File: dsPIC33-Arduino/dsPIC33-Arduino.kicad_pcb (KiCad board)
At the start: 2 copper layers, 68.6 x 53.3 mm, 8 parts, among them P1 Power, P2 Analog, P3 Digital, P4 Digital, P5 CONN_1, P6 CONN_1, P7 CONN_1, P8 CONN_1

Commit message: wip
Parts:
- added C1: 100nF, Capacitors_SMD:C_0805_HandSoldering, F.Cu at (118.7, 97.0)
- added C10: 100nF, Capacitors_ThroughHole:C_Disc_D3_P2.5, F.Cu at (138.2, 97.0)
- added C11: CP, w_capacitors:CP_4x5mm, F.Cu at (161.2, 92.4)
- added C12: 22pF, Capacitors_ThroughHole:C_Disc_D3_P2.5, F.Cu at (157.3, 114.7)
- added C13: 22pF, Capacitors_ThroughHole:C_Disc_D3_P2.5, F.Cu at (162.4, 114.4)
- added C14: 100nF, Capacitors_SMD:C_0805_HandSoldering, F.Cu at (115.3, 104.4)
- added C15: 100nF, Capacitors_SMD:C_0805_HandSoldering, F.Cu at (115.1, 109.1)
- added C2: 4,7uF, Capacitors_SMD:C_0805_HandSoldering, F.Cu at (118.7, 99.3)
- added C3: 10nF, Capacitors_SMD:C_0805_HandSoldering, F.Cu at (126.8, 84.7)
- added C4: 47pF, Capacitors_SMD:C_0805_HandSoldering, F.Cu at (124.1, 92.8)
- added C5: 47pF, Capacitors_SMD:C_0805_HandSoldering, F.Cu at (123.9, 95.0)
- added C6: 100nF, Capacitors_SMD:C_0805_HandSoldering, F.Cu at (124.9, 80.8)
- added C7: 100nF, Capacitors_SMD:C_0805_HandSoldering, F.Cu at (124.0, 97.4)
- added C8: 100nF, Capacitors_SMD:C_0805_HandSoldering, F.Cu at (127.5, 94.5)
- added C9: 100nF, Capacitors_ThroughHole:C_Disc_D3_P2.5, F.Cu at (132.8, 124.3)
- added CON1: BARREL_JACK, Connect:BARREL_JACK, F.Cu at (115.3, 118.7)
- added D1: RX LED, LEDs:LED_0805, F.Cu at (135.8, 78.7)
- added D2: TX LED, LEDs:LED_0805, F.Cu at (135.8, 80.6)
- added D3: Power LED, LEDs:LED-3MM, F.Cu at (142.1, 81.4)
- added D4: BAT43, w_pth_diodes:diode_do35, F.Cu at (141.7, 116.5)
- added D5: LED, LEDs:LED-3MM, F.Cu at (166.8, 93.0)
- added D6: D, w_pth_diodes:diode_do35, F.Cu at (141.7, 110.0)
- added F1: Ferrit, Resistors_SMD:R_0805_HandSoldering, F.Cu at (118.4, 80.5)
- added JP1: ICSP, ICSP:ICSP, F.Cu at (134.9, 116.0)
- added P10: CONN_01X03, Pin_Headers:Pin_Header_Straight_1x03, F.Cu at (175.8, 106.6)
- added P11: CONN_01X03, Pin_Headers:Pin_Header_Straight_1x03, F.Cu at (152.0, 91.1)
- added P12: CONN_01X04, Socket_Strips:Socket_Strip_Straight_1x04, F.Cu at (130.5, 112.5)
- added P13: CONN_01X02, Socket_Strips:Socket_Strip_Straight_2x01, F.Cu at (172.7, 117.0)
- added P14: Power Select, Socket_Strips:Socket_Strip_Straight_1x03, F.Cu at (140.2, 89.9)
- added P15: Grove I2C, w_conn_jst-ph:s4b-ph-kl, F.Cu at (173.2, 83.2)
- added P9: USB_B, Connect:USB_B, F.Cu at (119.4, 89.5)
- added R1: 27, Resistors_SMD:R_0805_HandSoldering, F.Cu at (123.6, 82.4)
- added R10: 0, Resistors_SMD:R_0805_HandSoldering, F.Cu at (124.0, 99.7)
- added R2: 27, Resistors_SMD:R_0805_HandSoldering, F.Cu at (132.1, 84.8)
- added R3: 270, Resistors_SMD:R_0805_HandSoldering, F.Cu at (131.4, 78.7)
- added R4: 270, Resistors_SMD:R_0805_HandSoldering, F.Cu at (131.4, 80.6)
- added R5: 1k5, w_pth_resistors:RC03, F.Cu at (141.9, 92.9)
- added R6: 470, w_pth_resistors:RC03, F.Cu at (141.7, 118.9)
- added R7: 4k7, w_pth_resistors:RC03, F.Cu at (142.0, 112.3)
- added R8: 4k7, Resistors_SMD:R_0805_HandSoldering, F.Cu at (129.5, 101.1)
- added R9: 1k5, w_pth_resistors:RC03, F.Cu at (167.9, 96.2)
- added SW1: SW_PUSH, Buttons_Switches_ThroughHole:SW_PUSH_SMALL, F.Cu at (117.1, 76.8)
- added U1: FT230XS, w_smd_dil:ssop-16, F.Cu at (125.4, 88.5)
- added U2: LM1117 3V3, TO_SOT_Packages_SMD:SOT-223, F.Cu at (122.3, 108.6)
- added U3: dsPIC33EVxxxGM102-I/SP, w_pth_circuits:dil_28-300_socket, F.Cu at (154.6, 102.9)
- added U4: 74LVC1G32, TO_SOT_Packages_SMD:SOT-353, F.Cu at (125.9, 103.0)
- added U5: LM1117 5V, TO_SOT_Packages_SMD:SOT-223, F.Cu at (128.3, 118.5)
- added Y1: Crystal, w_crystal:crystal_hc-49s, F.Cu at (159.8, 111.0)
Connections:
- net /A4(SDA) renamed /SDA
- net /A5(SCL) renamed /SCL
- P1 pad 2: /IOREF -> VDD
- P1 pad 3: /Reset -> /~RESET~
- P1 pad 8: /Vin -> +5V
- P4 pad 7: /1(Tx) -> /TX
- P4 pad 8: /0(Rx) -> /RX

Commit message: wip
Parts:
- added P16: PIN19, Pin_Headers:Pin_Header_Straight_1x03, F.Cu at (156.7, 93.3)
- added P17: UART/CAN, w_conn_jst-ph:s4b-ph-kl, F.Cu at (173.2, 82.5)
- P10: value CONN_01X03 -> PIN20
- P11: value CONN_01X03 -> PIN5
- P12: value CONN_01X04 -> PWR_IN; footprint Socket_Strips:Socket_Strip_Straight_1x04 -> Pin_Headers:Pin_Header_Straight_1x03
- P13: value CONN_01X02 -> PIN2
- P15: value Grove I2C -> I2C
- moved P13 48.7 mm to (134.1, 87.2), turned to 270 degrees
- moved JP1 40.1 mm to (173.2, 104.1)
- moved P10 28.5 mm to (152.9, 89.5), turned to 90 degrees
- moved P15 27.9 mm to (173.2, 111.1)
- moved C9 22.1 mm to (132.6, 102.2), turned to 270 degrees
- moved R9 20.2 mm to (165.0, 116.2), turned to 90 degrees
- moved P11 19.3 mm to (144.0, 108.6)
- moved D5 14.3 mm to (166.2, 107.3), turned to 270 degrees
- moved P14 12.4 mm to (132.6, 99.7), turned to 90 degrees
- moved R8 8.46 mm to (121.2, 102.2)
- moved D6 7.33 mm to (134.5, 111.1), turned to 90 degrees
- moved P12 7.28 mm to (129.5, 105.3), turned to 0 degrees
- moved D4 7.11 mm to (137.0, 111.1), turned to 90 degrees
- moved Y1 3.05 mm to (158.0, 108.6)
- moved C10 3.00 mm to (136.4, 94.6)
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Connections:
- P15 pad 1: /SCL -> GND
- P15 pad 2: /SDA -> VDD
- P15 pad 3: VDD -> /SDA
- P15 pad 4: GND -> /SCL
- U3 pad 19: GND -> Net-(P16-Pad2)
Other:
- board text added: "GND"
- board text added: "RX"
- board text added: "SCL"
- board text added: "SDA"
- board text added: "TX"
- board text added: "VDD"

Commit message: wip
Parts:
- D6: value D -> BAT43
- P13: footprint Socket_Strips:Socket_Strip_Straight_2x01 -> Pin_Headers:Pin_Header_Straight_1x02
- P14: footprint Socket_Strips:Socket_Strip_Straight_1x03 -> Pin_Headers:Pin_Header_Straight_1x03
- moved C9 31.0 mm to (163.1, 108.1), turned to 0 degrees
- moved R8 22.5 mm to (134.7, 84.3)
- moved C8 22.1 mm to (133.9, 115.7), turned to 270 degrees
- moved C2 20.9 mm to (124.3, 79.2)
- moved D6 20.6 mm to (137.7, 90.8)
- moved U5 17.8 mm to (115.6, 105.5), turned to 90 degrees
- moved U4 17.6 mm to (134.5, 87.6)
- moved C1 16.4 mm to (124.3, 81.5)
- moved C7 16.4 mm to (133.9, 110.5), turned to 90 degrees
- moved F1 15.4 mm to (124.2, 94.7), turned to 180 degrees
- moved C10 15.2 mm to (151.5, 93.5)
- moved P11 15.1 mm to (143.4, 93.5)
- moved C6 12.7 mm to (127.8, 93.2), turned to 270 degrees
- moved P12 11.7 mm to (120.5, 97.8), turned to 90 degrees
- moved R10 10.5 mm to (113.8, 97.3)
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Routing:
- net Net-(P9-Pad5): track 0.00 -> 16.1 mm
- net Net-(C5-Pad1): track 0.00 -> 8.25 mm
- net Net-(C3-Pad1): track 0.00 -> 7.11 mm
- net Net-(C4-Pad1): track 0.00 -> 6.25 mm
- net Net-(R1-Pad1): track 0.00 -> 1.90 mm
- net Net-(R2-Pad1): track 0.00 -> 1.72 mm
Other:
- net class Default: trace_width 0.25 -> 0.3048
- net class PWR1 added: clearance 0.2, trace_width 1.016, via_dia 0.8, via_drill 0.5

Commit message: wip
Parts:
- moved D1 1.98 mm to (135.9, 80.6)
- moved R3 1.94 mm to (131.6, 80.6)
- moved R4 1.91 mm to (131.6, 78.7)
- moved D2 1.91 mm to (135.9, 78.7)
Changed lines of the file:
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@@
     (links 139)
     (no_connects 129)
-    (area 110.922999 72.949999 179.653001 126.440001)
+    (area 90.283716 26.365 210.998001 134.065001)
     (thickness 1.6)
     (drawings 39)
@@
   )
   (module LEDs:LED_0805 (layer F.Cu)
-    (at 135.7884 78.6638)
+    (at 135.89 80.645)
     (descr "LED 0805 smd package")
     (tags "LED 0805 SMD")
@@
   )
   (module LEDs:LED_0805 (layer F.Cu)
-    (at 135.8392 80.645)
+    (at 135.89 78.74)
     (descr "LED 0805 smd package")
     (tags "LED 0805 SMD")
@@
   )
   (module Resistors_SMD:R_0805_HandSoldering (layer F.Cu)
-    (at 131.4196 78.7146 180)
+    (at 131.572 80.645 180)
     (descr "Resistor SMD 0805, hand soldering")
     (tags "resistor 0805")
@@
   )
   (module Resistors_SMD:R_0805_HandSoldering (layer F.Cu)
-    (at 131.4196 80.645 180)
+    (at 131.572 78.74 180)
     (descr "Resistor SMD 0805, hand soldering")
     (tags "resistor 0805")
@@
   (segment (start 117.38102 86.995) (end 118.495421 85.880599) (width 0.3048) (layer F.Cu) (net 29))
   (segment (start 118.495421 85.880599) (end 121.059599 85.880599) (width 0.3048) (layer F.Cu) (net 29))
-  (segment (start 114.681 94.26448) (end 114.681 82.26552) (width 0.3048) (layer F.Cu) (net 51) (status C00000))
-  (segment (start 114.681 94.26448) (end 114.39652 94.26448) (width 0.3048) (layer F.Cu) (net 51) (status C00000))
-  (segment (start 114.39652 94.26448) (end 112.442 96.219) (width 0.3048) (layer F.Cu) (net 51) (status 400000))
-  (segment (start 112.442 96.219) (end 112.442 97.282) (width 0.3048) (layer F.Cu) (net 51) (status 800000))
+  (segment (start 114.681 94.26448) (end 114.681 82.26552) (width 0.3048) (layer F.Cu) (net 51))
+  (segment (start 114.681 94.26448) (end 114.39652 94.26448) (width 0.3048) (layer F.Cu) (net 51))
+  (segment (start 114.39652 94.26448) (end 112.442 96.219) (width 0.3048) (layer F.Cu) (net 51))
+  (segment (start 112.442 96.219) (end 112.442 97.282) (width 0.3048) (layer F.Cu) (net 51))
   (segment (start 125.556 90.297) (end 126.5555 90.297) (width 0.3048) (layer F.Cu) (net 55))
   (segment (start 126.5555 90.297) (end 127.1905 89.662) (width 0.3048) (layer F.Cu) (net 55))

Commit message: wip
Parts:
- C14, C15, C7, C8: footprint Capacitors_SMD:C_0805_HandSoldering -> Capacitors_ThroughHole:C_Disc_D3_P2.5
- P17: value UART/CAN -> UART
- SW1: footprint Buttons_Switches_ThroughHole:SW_PUSH_SMALL -> w_switch:PCB_PUSH
- U5: value LM1117 5V -> 7805; footprint TO_SOT_Packages_SMD:SOT-223 -> 78xx:TO-252-2Lead
- moved P11 19.6 mm to (142.7, 113.0), turned to 180 degrees
- moved P12 18.0 mm to (130.1, 113.1), turned to 180 degrees
- moved C8 17.2 mm to (123.0, 102.4)
- moved U2 16.4 mm to (116.7, 102.2)
- moved C7 15.7 mm to (122.3, 99.9), turned to 0 degrees
- moved C14 11.6 mm to (124.4, 114.7), turned to 90 degrees
- moved C11 11.4 mm to (151.0, 93.3)
- moved R7 7.65 mm to (136.4, 113.0)
- moved U5 7.17 mm to (121.0, 110.2)
- moved P10 6.99 mm to (145.9, 89.4)
- moved R9 6.59 mm to (160.9, 111.1)
- moved D4 5.43 mm to (136.4, 108.0)
- moved R6 5.43 mm to (136.4, 110.5)
- moved R10 5.12 mm to (118.7, 95.7)
- moved C10 4.32 mm to (147.2, 93.3), turned to 180 degrees
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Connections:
- C14 pad 1: Net-(C14-Pad1) -> /VI
- CON1 pad 1: Net-(C14-Pad1) -> /VI
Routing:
- net Net-(P9-Pad5): track 16.1 -> 12.3 mm
- net Net-(R1-Pad1): track 1.90 -> 0.00 mm
- net Net-(R2-Pad1): track 1.72 -> 0.00 mm
- added copper zone on B.Cu, net GND
- added copper zone on F.Cu, net GND
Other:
- net class PWR2 added: clearance 0.2, trace_width 0.508, via_dia 0.6, via_drill 0.4
- board text added: "3V3"
- board text added: "5V"
- board text added: "A0 RPI16"
- board text added: "A1 RPI17"
- board text added: "A2 RPI32"
- board text added: "A3"
- board text added: "A3 RPI33"
- board text added: "CAP"
- board text added: "D0 RX"
- board text added: "D1 TX"
- board text added: "D10 RPI45"
- board text added: "D11 RPI46"
- board text added: "D12 RPI47"
- board text added: "D13 RP20"
- board text added: "D2 RP36"
- board text added: "D3"
- board text added: "D3 RPI33"
- board text added: "D4 RP39"
- board text added: "D5 RP40"
- board text added: "D6 RP41"
- board text added: "D7 RP42"
- board text added: "D8 RP43"
- board text added: "D9 RPI44"
- board text added: "Pin19"
- board text added: "Pin20"
- board text added: "Pin5"
- board text added: "Reset"
- board text added: "SCL RPI34"
- board text added: "SDA RP35"

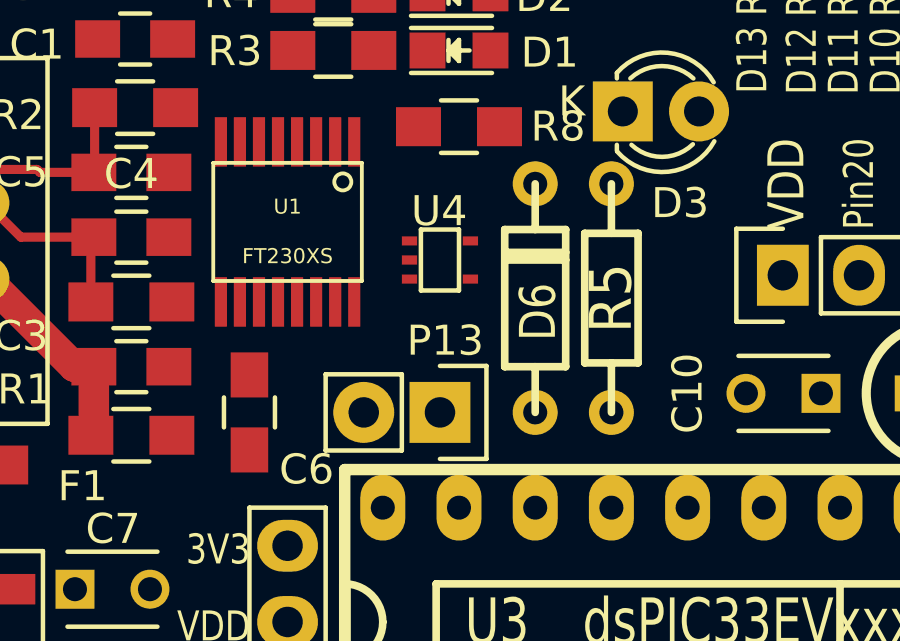
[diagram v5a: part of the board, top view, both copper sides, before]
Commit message: use diode the right way
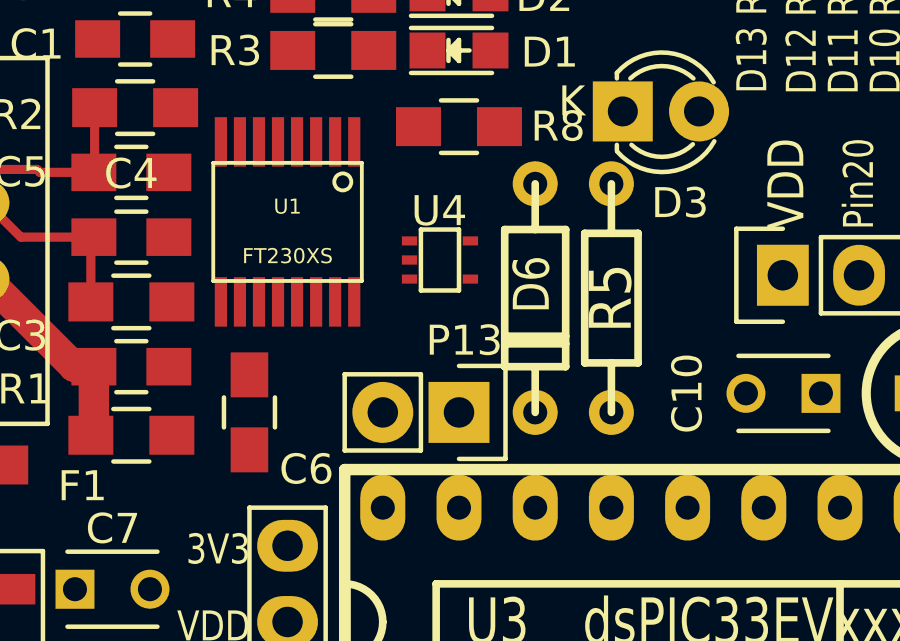
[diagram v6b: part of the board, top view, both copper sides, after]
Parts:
- moved P13 0.63 mm to (135.1, 94.0)
- turned D6 to 270 degrees
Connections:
- D6 pad 1: /~MCLR~ -> Net-(D6-Pad1)
- D6 pad 2: Net-(D6-Pad2) -> /~MCLR~
- U3 pad 14: /RX -> /SDA
- U3 pad 15: /TX -> /SCL
- U3 pad 21: /7 -> /10(**/SS)
- U3 pad 22: /8 -> /11(**/MOSI)
- U3 pad 23: /9(**) -> /12(MISO)
- U3 pad 24: /10(**/SS) -> /7
- U3 pad 25: /11(**/MOSI) -> /8
- U3 pad 26: /12(MISO) -> /9(**)
- U3 pad 6: /SCL -> /RX
- U3 pad 7: /SDA -> /TX
- U4 pad 4: Net-(D6-Pad2) -> Net-(D6-Pad1)

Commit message: wip
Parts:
- C11: value CP -> 10uF ESR
- C14, C15, C7: value 100nF -> 47uF; footprint Capacitors_ThroughHole:C_Disc_D3_P2.5 -> w_capacitors:CP_4x5mm
- moved C7 1.66 mm to (123.7, 98.9)
- moved C15 1.62 mm to (125.6, 108.7), turned to 180 degrees
- moved C8 0.85 mm to (123.8, 102.5)
- moved C14 0.84 mm to (125.2, 114.9), turned to 270 degrees
- moved P14 0.25 mm to (129.7, 103.5)
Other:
- board text added: "A3 *RPI33"
- board text added: "BJ"
- board text added: "D10 RP42"
- board text added: "D11 RP43"
- board text added: "D12 RPI44"
- board text added: "D3 *RPI33"
- board text added: "D7 RPI45"
- board text added: "D8 RPI46"
- board text added: "D9 RPI47"
- board text added: "SCL RP38"
- board text added: "SDA RP37"
- board text added: "USB"
- board text removed: "D10 RPI45"
- board text removed: "D11 RPI46"
- board text removed: "D12 RPI47"
- board text removed: "D7 RP42"
- board text removed: "D8 RP43"
- board text removed: "D9 RPI44"
- board text removed: "SCL RPI34"
- board text removed: "SDA RP35"

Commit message: wip
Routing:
- net /~RESET~: track 0.00 -> 59.6 mm, vias 0 -> 2
- net +5V: track 0.00 -> 57.6 mm
- net VDD: track 0.00 -> 57.1 mm
- net +3V3: track 0.00 -> 56.8 mm, vias 0 -> 1
- net VCC: track 0.00 -> 51.0 mm, vias 0 -> 2
- net Net-(C6-Pad1): track 0.00 -> 20.9 mm
- net /~MCLR~: track 0.00 -> 18.6 mm, vias 0 -> 2
- net Net-(C7-Pad1): track 0.00 -> 14.0 mm
- net /CTS: track 0.00 -> 10.8 mm, vias 0 -> 1
- net /RTS: track 0.00 -> 10.6 mm, vias 0 -> 2
- net /VI: track 0.00 -> 10.2 mm
- net Net-(R3-Pad2): track 0.00 -> 8.91 mm, vias 0 -> 2
- net Net-(C12-Pad1): track 0.00 -> 8.15 mm
- net Net-(C13-Pad1): track 0.00 -> 8.15 mm
- net Net-(R4-Pad2): track 0.00 -> 6.25 mm
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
